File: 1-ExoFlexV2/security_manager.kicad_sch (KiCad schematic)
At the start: 12 parts, among them U10 OR Gate, U11 OR Gate, U12 OR Gate, U13 OR Gate, U14 OR Gate, U15 OR Gate, U16 OR Gate, U17 OR Gate, U18 OR Gate, U19 OR Gate, U8 OR Gate, U9 OR Gate

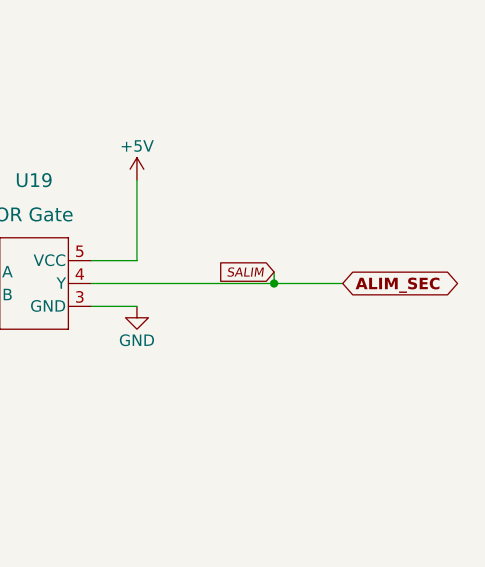
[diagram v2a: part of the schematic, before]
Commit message: Bug NetList
- Ajout de net-tie pour les GND et et les +5V
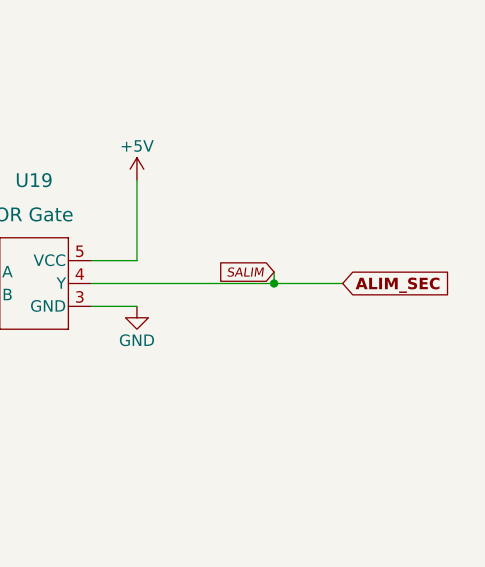
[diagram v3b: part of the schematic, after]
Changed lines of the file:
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@@
     )
   )
-  (global_label "ALIM_SEC" (shape bidirectional) (at 271.78 80.01 0) (fields_autoplaced)
+  (global_label "ALIM_SEC" (shape input) (at 271.78 80.01 0) (fields_autoplaced)
     (effects (font (size 1.27 1.27) (thickness 0.254) bold) (justify left))
     (property "Intersheet References" "${INTERSHEET_REFS}" (id 0) (at 283.343 79.883 0)
@@
   (symbol (lib_id "power:GND") (at 248.92 82.55 0) (unit 1)
     (in_bom yes) (on_board yes)
-    (property "Reference" "#PWR0159" (id 0) (at 248.92 88.9 0)
+    (property "Reference" "#PWR0160" (id 0) (at 248.92 88.9 0)
       (effects (font (size 1.27 1.27)) hide)
     )
@@
   (symbol (lib_id "power:GND") (at 64.77 148.59 0) (unit 1)
     (in_bom yes) (on_board yes)
-    (property "Reference" "#PWR0139" (id 0) (at 64.77 154.94 0)
+    (property "Reference" "#PWR0140" (id 0) (at 64.77 154.94 0)
       (effects (font (size 1.27 1.27)) hide)
     )
@@
   (symbol (lib_id "power:+5V") (at 66.04 78.74 0) (unit 1)
     (in_bom yes) (on_board yes)
-    (property "Reference" "#PWR0144" (id 0) (at 66.04 82.55 0)
+    (property "Reference" "#PWR0145" (id 0) (at 66.04 82.55 0)
       (effects (font (size 1.27 1.27)) hide)
     )
@@
   (symbol (lib_id "power:+5V") (at 107.95 142.24 0) (unit 1)
     (in_bom yes) (on_board yes)
-    (property "Reference" "#PWR0148" (id 0) (at 107.95 146.05 0)
+    (property "Reference" "#PWR0149" (id 0) (at 107.95 146.05 0)
       (effects (font (size 1.27 1.27)) hide)
     )
@@
   (symbol (lib_id "power:GND") (at 64.77 123.19 0) (unit 1)
     (in_bom yes) (on_board yes)
-    (property "Reference" "#PWR0137" (id 0) (at 64.77 129.54 0)
+    (property "Reference" "#PWR0138" (id 0) (at 64.77 129.54 0)
       (effects (font (size 1.27 1.27)) hide)
     )
@@
   (symbol (lib_id "power:GND") (at 107.95 100.33 0) (unit 1)
     (in_bom yes) (on_board yes)
-    (property "Reference" "#PWR0147" (id 0) (at 107.95 106.68 0)
+    (property "Reference" "#PWR0148" (id 0) (at 107.95 106.68 0)
       (effects (font (size 1.27 1.27)) hide)
     )
@@
   (symbol (lib_id "power:+5V") (at 125.73 30.48 0) (unit 1)
     (in_bom yes) (on_board yes)
-    (property "Reference" "#PWR0150" (id 0) (at 125.73 34.29 0)
+    (property "Reference" "#PWR0151" (id 0) (at 125.73 34.29 0)
       (effects (font (size 1.27 1.27)) hide)
     )
@@
   (symbol (lib_id "power:GND") (at 66.04 43.18 0) (unit 1)
     (in_bom yes) (on_board yes)
-    (property "Reference" "#PWR0141" (id 0) (at 66.04 49.53 0)
+    (property "Reference" "#PWR0142" (id 0) (at 66.04 49.53 0)
       (effects (font (size 1.27 1.27)) hide)
     )
@@
   (symbol (lib_id "power:+5V") (at 64.77 134.62 0) (unit 1)
     (in_bom yes) (on_board yes)
-    (property "Reference" "#PWR0138" (id 0) (at 64.77 138.43 0)
+    (property "Reference" "#PWR0139" (id 0) (at 64.77 138.43 0)
       (effects (font (size 1.27 1.27)) hide)
     )
@@
   (symbol (lib_id "power:GND") (at 125.73 44.45 0) (unit 1)
     (in_bom yes) (on_board yes)
-    (property "Reference" "#PWR0151" (id 0) (at 125.73 50.8 0)
+    (property "Reference" "#PWR0152" (id 0) (at 125.73 50.8 0)
       (effects (font (size 1.27 1.27)) hide)
     )
@@
   (symbol (lib_id "power:+5V") (at 248.92 68.58 0) (unit 1)
     (in_bom yes) (on_board yes)
-    (property "Reference" "#PWR0158" (id 0) (at 248.92 72.39 0)
+    (property "Reference" "#PWR0159" (id 0) (at 248.92 72.39 0)
       (effects (font (size 1.27 1.27)) hide)
     )
@@
   (symbol (lib_id "power:GND") (at 157.48 157.48 0) (unit 1)
     (in_bom yes) (on_board yes)
-    (property "Reference" "#PWR0155" (id 0) (at 157.48 163.83 0)
+    (property "Reference" "#PWR0156" (id 0) (at 157.48 163.83 0)
       (effects (font (size 1.27 1.27)) hide)
     )
@@
   (symbol (lib_id "power:GND") (at 107.95 156.21 0) (unit 1)
     (in_bom yes) (on_board yes)
-    (property "Reference" "#PWR0149" (id 0) (at 107.95 162.56 0)
+    (property "Reference" "#PWR0150" (id 0) (at 107.95 162.56 0)
       (effects (font (size 1.27 1.27)) hide)
     )
@@
   (symbol (lib_id "power:+5V") (at 107.95 86.36 0) (unit 1)
     (in_bom yes) (on_board yes)
-    (property "Reference" "#PWR0146" (id 0) (at 107.95 90.17 0)
+    (property "Reference" "#PWR0147" (id 0) (at 107.95 90.17 0)
       (effects (font (size 1.27 1.27)) hide)
     )
@@
   (symbol (lib_id "power:+5V") (at 66.04 29.21 0) (unit 1)
     (in_bom yes) (on_board yes)
-    (property "Reference" "#PWR0140" (id 0) (at 66.04 33.02 0)
+    (property "Reference" "#PWR0141" (id 0) (at 66.04 33.02 0)
       (effects (font (size 1.27 1.27)) hide)
     )
@@
   (symbol (lib_id "power:+5V") (at 64.77 109.22 0) (unit 1)
     (in_bom yes) (on_board yes)
-    (property "Reference" "#PWR0136" (id 0) (at 64.77 113.03 0)
+    (property "Reference" "#PWR0137" (id 0) (at 64.77 113.03 0)
       (effects (font (size 1.27 1.27)) hide)
     )
@@
   (symbol (lib_id "power:GND") (at 201.93 124.46 0) (unit 1)
     (in_bom yes) (on_board yes)
-    (property "Reference" "#PWR0157" (id 0) (at 201.93 130.81 0)
+    (property "Reference" "#PWR0158" (id 0) (at 201.93 130.81 0)
       (effects (font (size 1.27 1.27)) hide)
     )
@@
   (symbol (lib_id "power:+5V") (at 201.93 110.49 0) (unit 1)
     (in_bom yes) (on_board yes)
-    (property "Reference" "#PWR0156" (id 0) (at 201.93 114.3 0)
+    (property "Reference" "#PWR0157" (id 0) (at 201.93 114.3 0)
       (effects (font (size 1.27 1.27)) hide)
     )
@@
   (symbol (lib_id "power:+5V") (at 66.04 54.61 0) (unit 1)
     (in_bom yes) (on_board yes)
-    (property "Reference" "#PWR0142" (id 0) (at 66.04 58.42 0)
+    (property "Reference" "#PWR0143" (id 0) (at 66.04 58.42 0)
       (effects (font (size 1.27 1.27)) hide)
     )
@@
   (symbol (lib_id "power:GND") (at 157.48 101.6 0) (unit 1)
     (in_bom yes) (on_board yes)
-    (property "Reference" "#PWR0153" (id 0) (at 157.48 107.95 0)
+    (property "Reference" "#PWR0154" (id 0) (at 157.48 107.95 0)
       (effects (font (size 1.27 1.27)) hide)
     )
@@
   (symbol (lib_id "power:GND") (at 66.04 92.71 0) (unit 1)
     (in_bom yes) (on_board yes)
-    (property "Reference" "#PWR0145" (id 0) (at 66.04 99.06 0)
+    (property "Reference" "#PWR0146" (id 0) (at 66.04 99.06 0)
       (effects (font (size 1.27 1.27)) hide)
     )
@@
   (symbol (lib_id "power:+5V") (at 157.48 143.51 0) (unit 1)
     (in_bom yes) (on_board yes)
-    (property "Reference" "#PWR0154" (id 0) (at 157.48 147.32 0)
+    (property "Reference" "#PWR0155" (id 0) (at 157.48 147.32 0)
       (effects (font (size 1.27 1.27)) hide)
     )
@@
   (symbol (lib_id "power:+5V") (at 157.48 87.63 0) (unit 1)
     (in_bom yes) (on_board yes)
-    (property "Reference" "#PWR0152" (id 0) (at 157.48 91.44 0)
+    (property "Reference" "#PWR0153" (id 0) (at 157.48 91.44 0)
       (effects (font (size 1.27 1.27)) hide)
     )
@@
   (symbol (lib_id "power:GND") (at 66.04 68.58 0) (unit 1)
     (in_bom yes) (on_board yes)
-    (property "Reference" "#PWR0143" (id 0) (at 66.04 74.93 0)
-      (effects (font (size 1.27 1.27)) hide)
-    )
+    (property "Reference" "#PWR0144" (id 0) (at 66.04 74.93 0)
+      (effects (font (size 1.27 1.27)) hide)
+    )

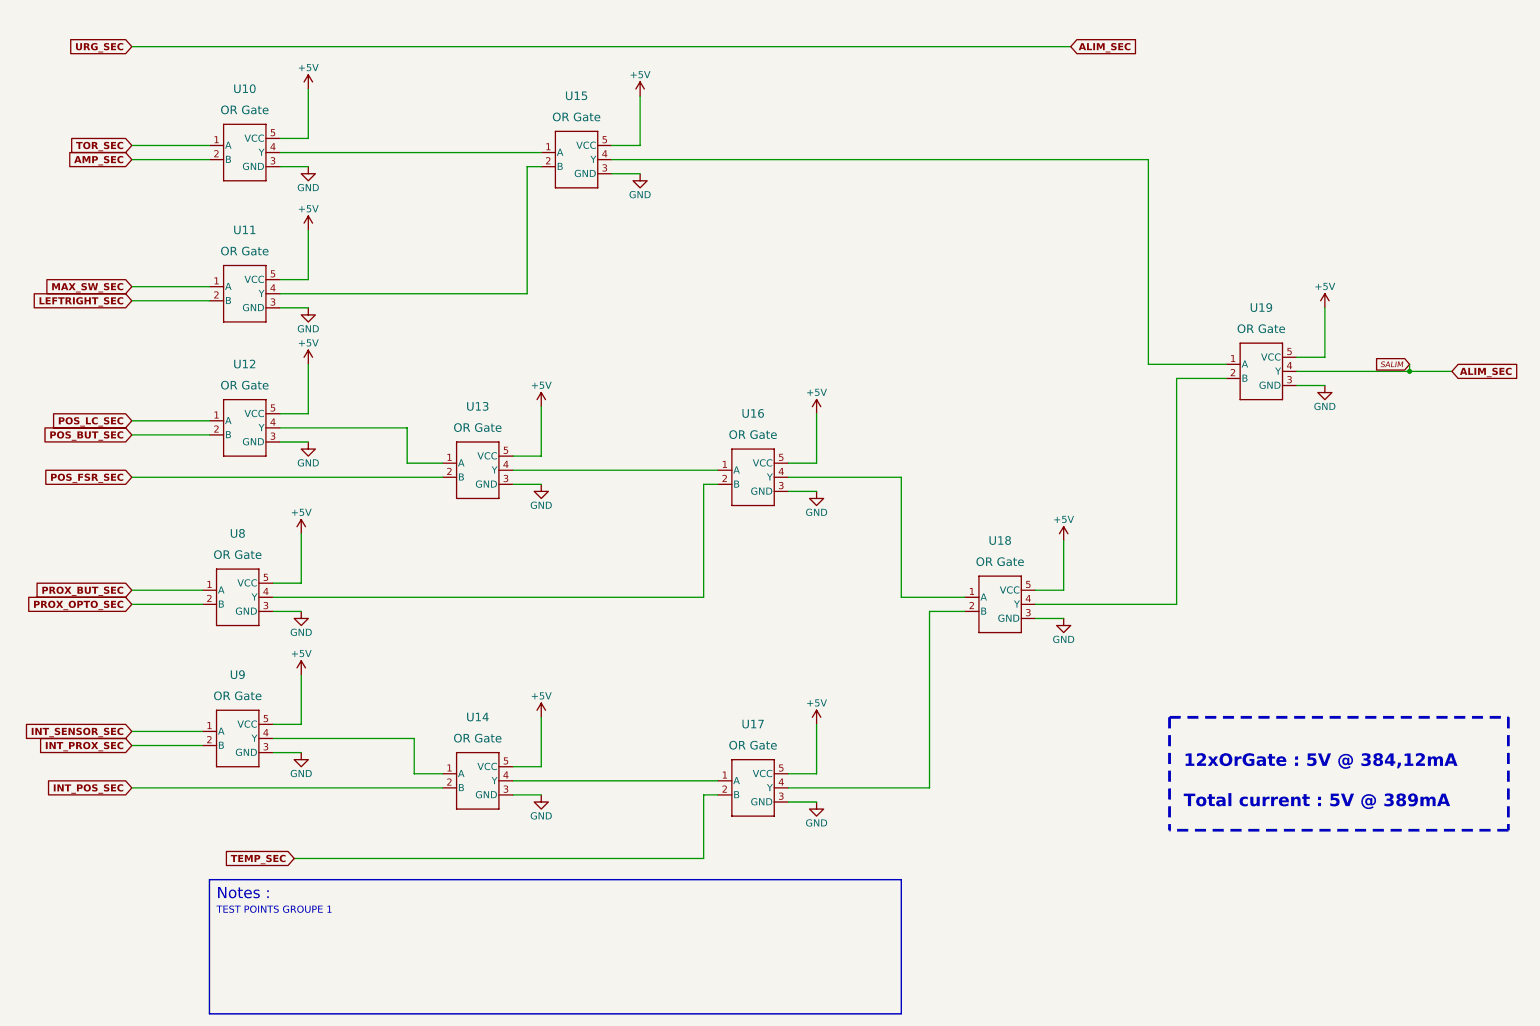
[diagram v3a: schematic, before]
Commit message: Finalisation 3
- Changement des régulateur de tension
- Retrait de test point inutile
- Changement de jumper mal positionner
- Ajout de Mounting holes et fiducial
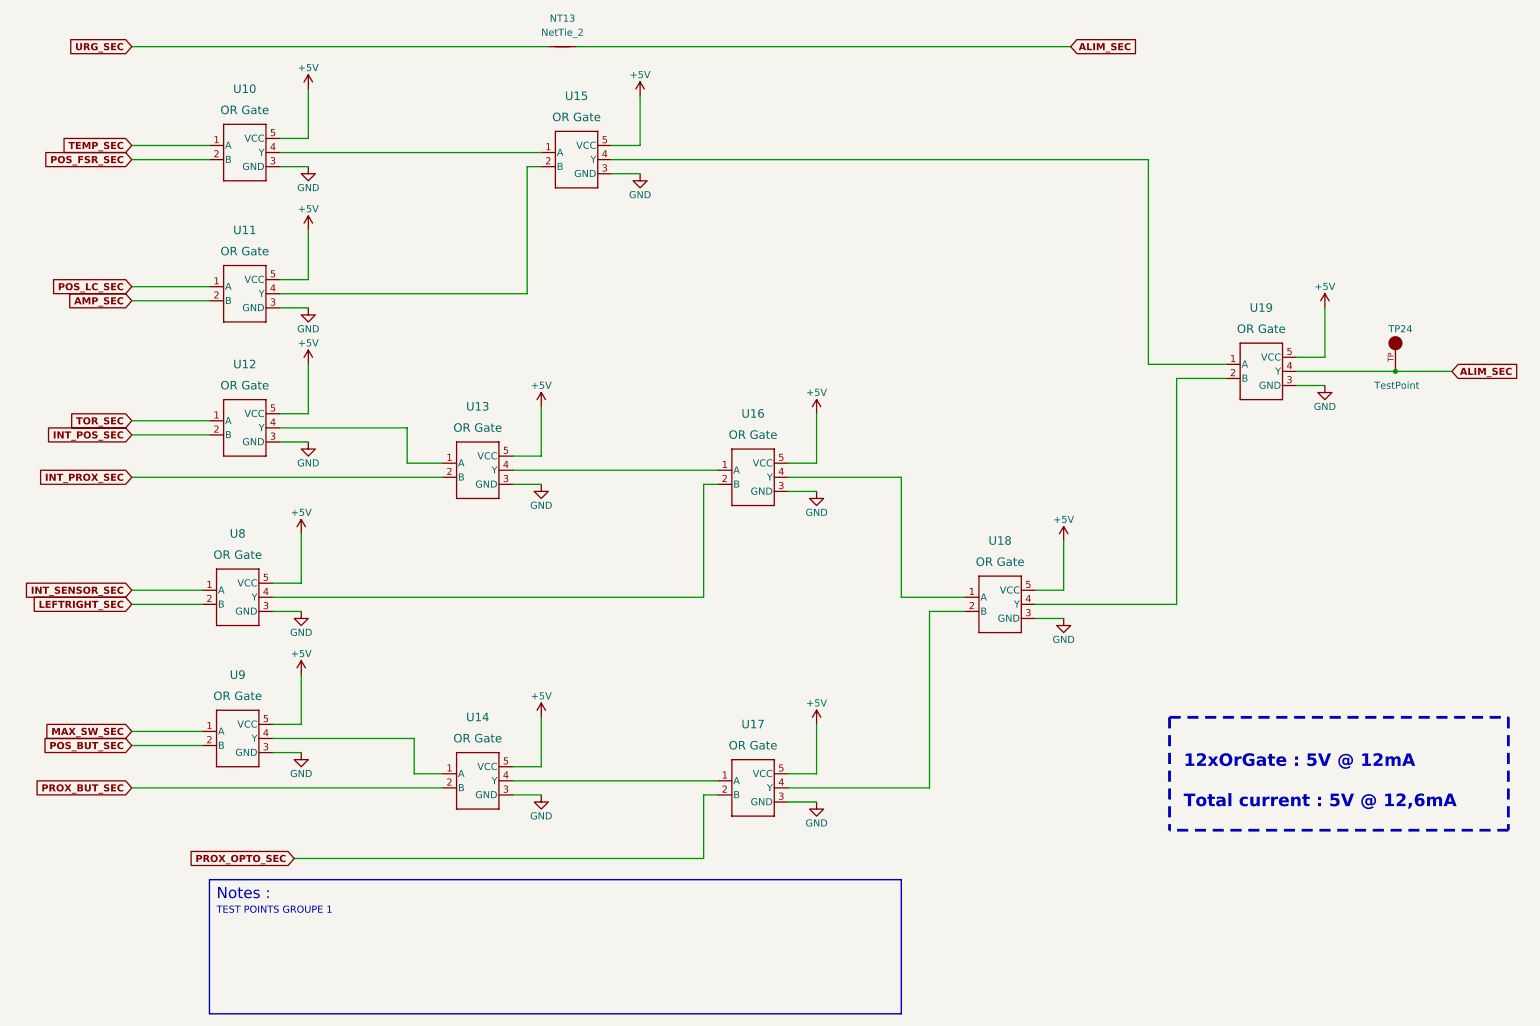
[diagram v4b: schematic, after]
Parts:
- added NT13: NetTie_2, NetTie:NetTie-2_THT_Pad0.3mm, symbol Device:NetTie_2
- added TP24: TestPoint, FootPrint:KEYSTONE_5005, symbol SymLib:5005
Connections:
- net ALIM_SEC: now also NT13.2, TP24.TP
- net AMP_SEC: now also U11.2 (B); no longer U10.2 (B)
- net INT_POS_SEC: now also U12.2 (B); no longer U14.2 (B)
- net INT_PROX_SEC: now also U13.2 (B); no longer U9.2 (B)
- net INT_SENSOR_SEC: now also U8.1 (A); no longer U9.1 (A)
- net LEFTRIGHT_SEC: now also U8.2 (B); no longer U11.2 (B)
- net MAX_SW_SEC: now also U9.1 (A); no longer U11.1 (A)
- net POS_BUT_SEC: now also U9.2 (B); no longer U12.2 (B)
- net POS_FSR_SEC: now also U10.2 (B); no longer U13.2 (B)
- net POS_LC_SEC: now also U11.1 (A); no longer U12.1 (A)
- net PROX_BUT_SEC: now also U14.2 (B); no longer U8.1 (A)
- net PROX_OPTO_SEC: now also U17.2 (B); no longer U8.2 (B)
- net TEMP_SEC: now also U10.1 (A); no longer U17.2 (B)
- net TOR_SEC: now also U12.1 (A); no longer U10.1 (A)
- new net URG_SEC: NT13.1
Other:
- note added: "12xOrGate : 5V @ 12mA Total current : 5V @ 12,6mA"
- note removed: "12xOrGate : 5V @ 384,12mA Total current : 5V @ 389mA"

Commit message: Finalisation schéma FIN
- Changement des uméro pour les inverseurs
- Changement des connecteur et début de placement
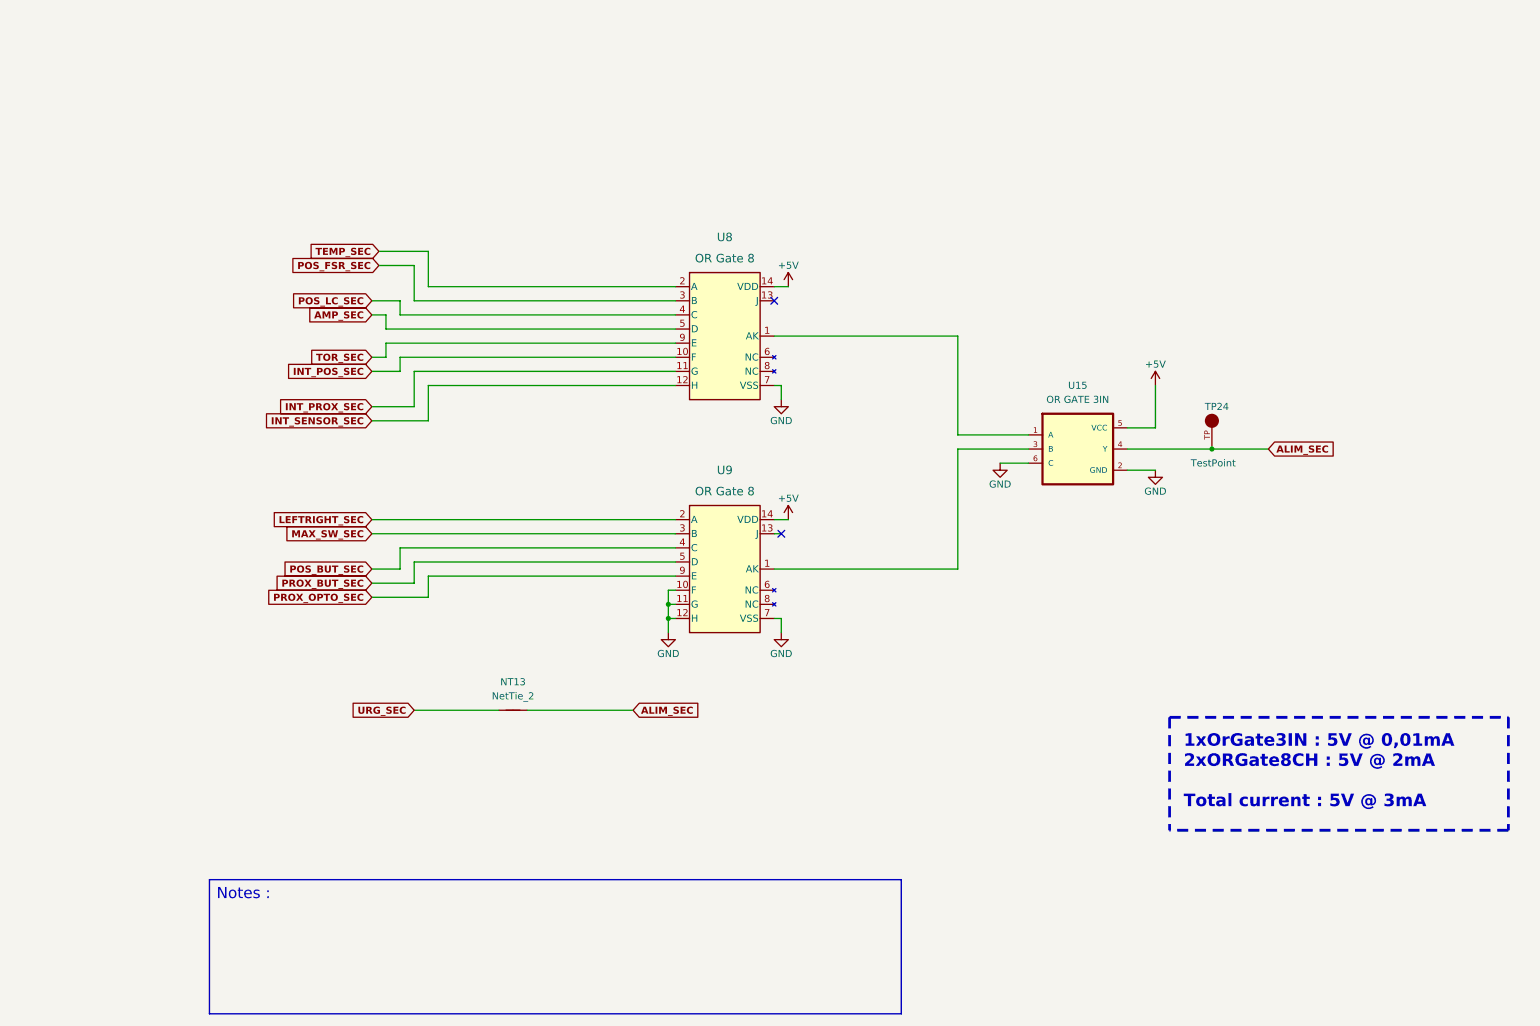
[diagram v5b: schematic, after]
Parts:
- removed U10, U11, U12, U13, U14, U15, U16, U17, U18, U19, U8, U9: OR Gate, FootPrint:SOT95P270X145-5N, symbol SymLib:SN74LVC1G32DBVR
- added U15: OR GATE 3IN, FootPrintLib:SOT95P280X145-6N, symbol SymLib:SN74LVC1G332DBVR
- added U8, U9: OR Gate 8, FootPrint:D14, symbol SymLib:CD4078BM96
- TP24: NOTES (none) -> DO NOT POPULATE; PURCHASE-URL https://pricing.snapeda.com/search/part/5005/?ref=eda -> (none)
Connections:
- net +5V: now also U15.5 (VCC), U8.14 (VDD), U9.14 (VDD)
- net ALIM_SEC: now also U15.4 (Y)
- net AMP_SEC: now also U8.5 (D)
- net GND: now also U15.2 (GND), U15.6 (C), U8.7 (VSS), U9.10 (F), U9.11 (G), U9.12 (H), U9.7 (VSS)
- net INT_POS_SEC: now also U8.10 (F)
- net INT_PROX_SEC: now also U8.11 (G)
- net INT_SENSOR_SEC: now also U8.12 (H)
- net LEFTRIGHT_SEC: now also U9.2 (A)
- net MAX_SW_SEC: now also U9.3 (B)
- net POS_BUT_SEC: now also U9.4 (C)
- net POS_FSR_SEC: now also U8.3 (B)
- net POS_LC_SEC: now also U8.4 (C)
- net PROX_BUT_SEC: now also U9.5 (D)
- net PROX_OPTO_SEC: now also U9.9 (E)
- net TEMP_SEC: now also U8.2 (A)
- net TOR_SEC: now also U8.9 (E)
- new net: U15.3 (B), U9.1 (AK)
- new net: U15.1 (A), U8.1 (AK)
- no-connect marks 0 -> 2
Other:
- note added: "1xOrGate3IN : 5V @ 0,01mA 2xORGate8CH : 5V @ 2mA Total current : 5V @ 3mA"
- note removed: "12xOrGate : 5V @ 12mA Total current : 5V @ 12,6mA"
- note removed: "TEST POINTS GROUPE 1"
- moved on the sheet: NT13, TP24
